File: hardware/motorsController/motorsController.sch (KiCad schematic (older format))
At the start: 10 parts, among them J1 batery_connector, J2 Screw_Terminal_01x01, J3 Screw_Terminal_01x01, J4 Screw_Terminal_01x01, J5 Screw_Terminal_01x01, J6 Screw_Terminal_01x01, J7 Screw_Terminal_01x01, J8 Screw_Terminal_01x01, J9 Screw_Terminal_01x01

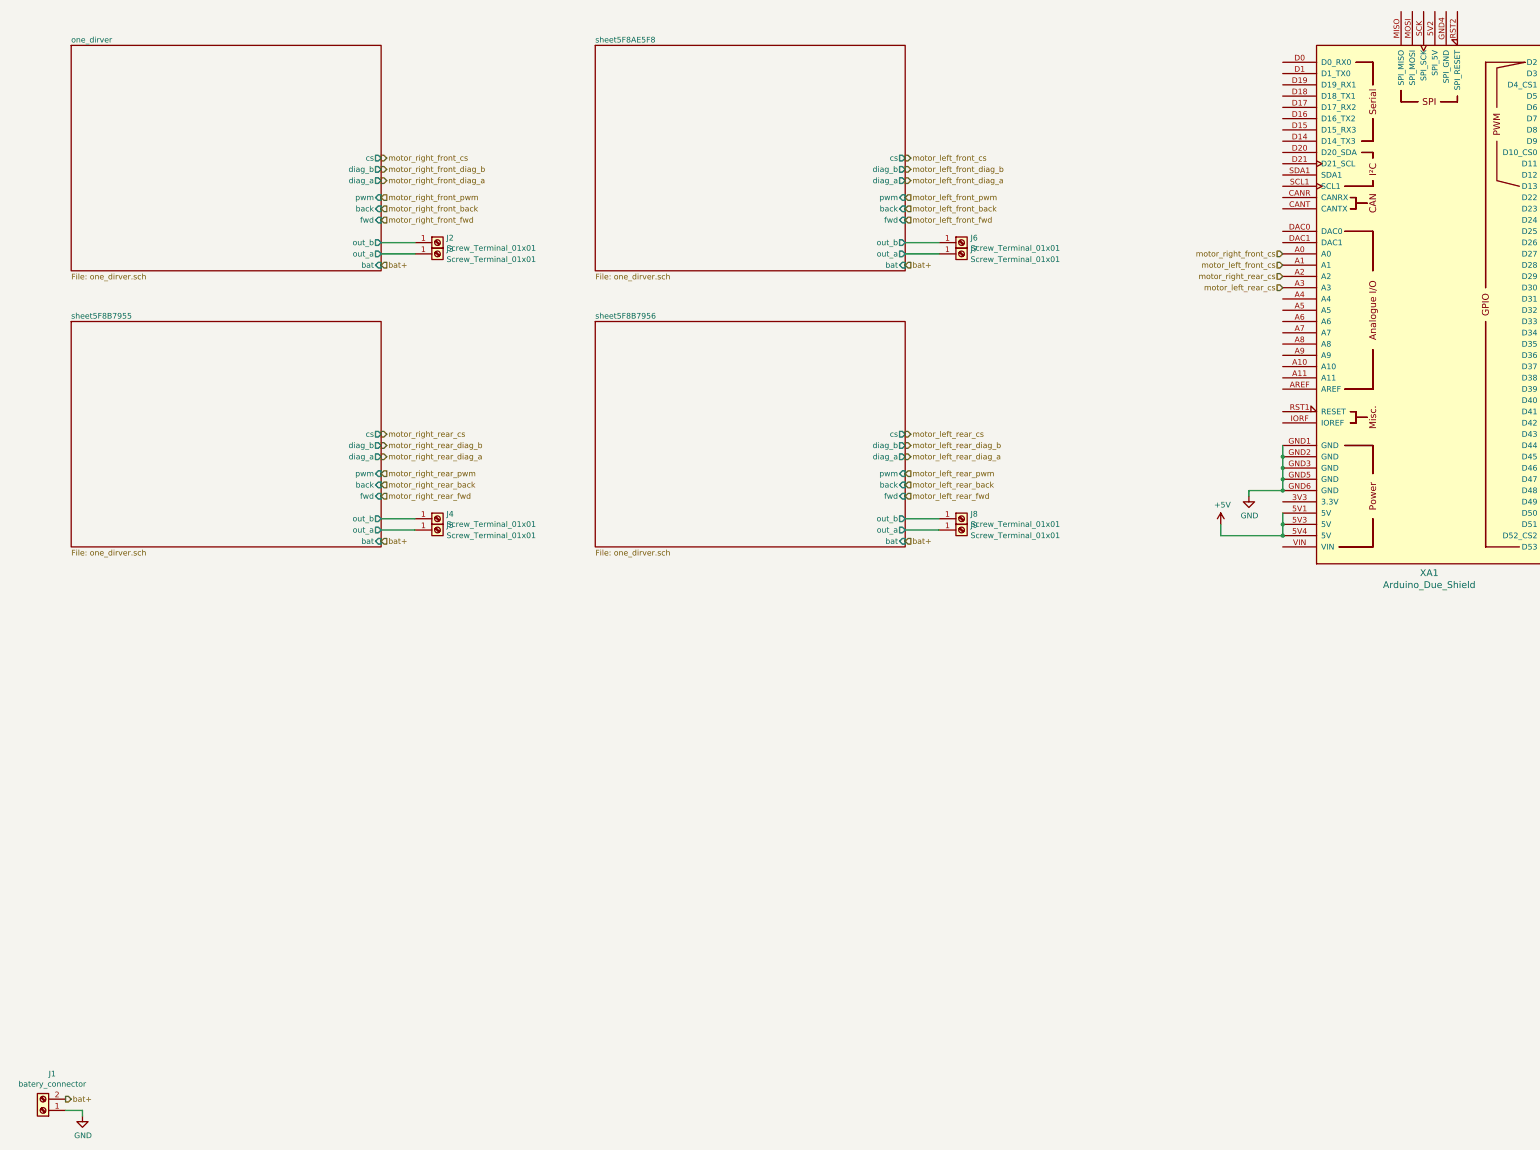
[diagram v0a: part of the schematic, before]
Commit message: layout and connect power for a pair of drivers
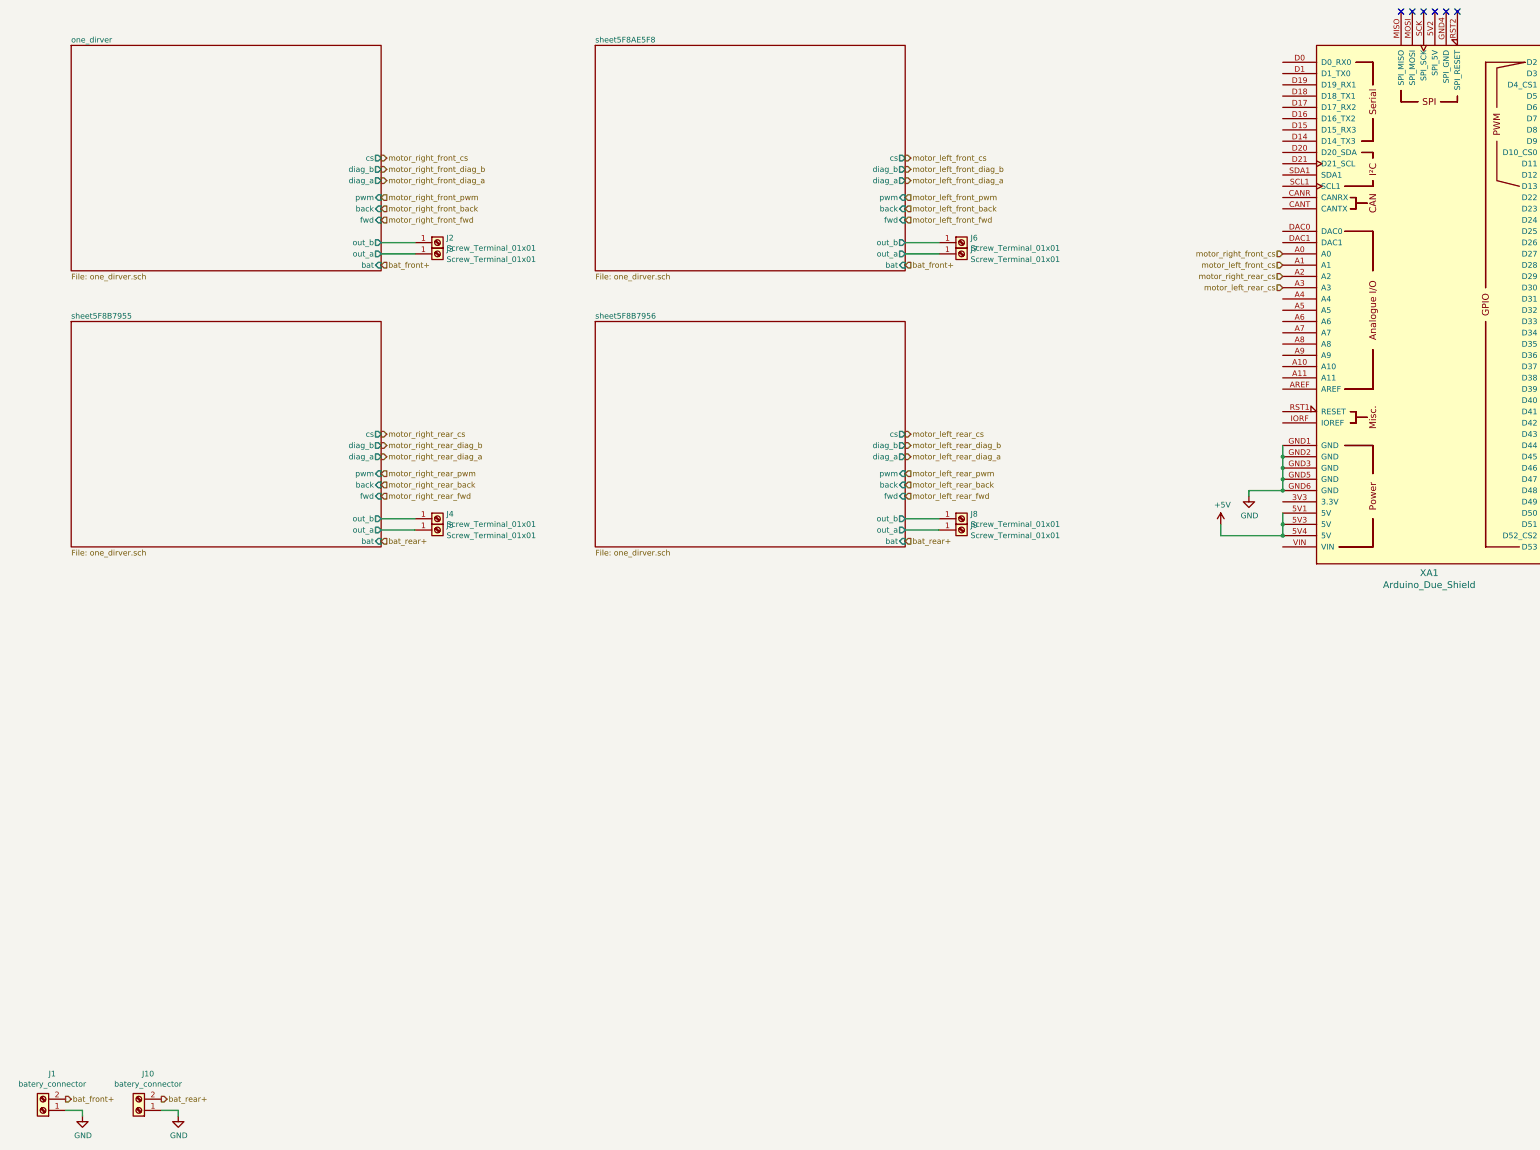
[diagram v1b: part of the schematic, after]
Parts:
- added J10: batery_connector, TerminalBlock:TerminalBlock_bornier-2_P5.08mm, symbol Connector:Screw_Terminal_01x02
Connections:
- net GND: now also J10.1 (Pin_1)
- net bat+ renamed bat_front+
- new net bat_rear+: J10.2 (Pin_2)
- no-connect marks 0 -> 6
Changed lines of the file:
@@
 	1350 10650 1200 10650
 Text HLabel 1200 10550 2    50   Output ~ 0
-bat+
+bat_front+
 Text HLabel 4000 3150 2    50   Input ~ 0
-bat+
+bat_front+
 $Comp
 L arduino:Arduino_Due_Shield XA1
@@
 motor_left_front_diag_a
 Text HLabel 8650 3150 2    50   Input ~ 0
-bat+
+bat_front+
 $Comp
 L Connector:Screw_Terminal_01x01 J6
@@
 motor_right_rear_diag_a
 Text HLabel 4000 5600 2    50   Input ~ 0
-bat+
+bat_rear+
 $Comp
 L Connector:Screw_Terminal_01x01 J4
@@
 motor_left_rear_diag_a
 Text HLabel 8650 5600 2    50   Input ~ 0
-bat+
+bat_rear+
 $Comp
 L Connector:Screw_Terminal_01x01 J8
@@
 Text HLabel 14600 1650 2    50   Output ~ 0
 motor_left_rear_pwm
+$Comp
+L Connector:Screw_Terminal_01x02 J10
+U 1 1 5F8FE7B8
+P 1850 10650
+F 0 "J10" H 1768 10325 50  0000 C CNN
+F 1 "batery_connector" H 1768 10416 50  0000 C CNN
+F 2 "TerminalBlock:TerminalBlock_bornier-2_P5.08mm" H 1850 10650 50  0001 C CNN
+F 3 "~" H 1850 10650 50  0001 C CNN
+	1    1850 10650
+	-1   0    0    1
+$EndComp
+$Comp
+L power:GND #PWR0120
+U 1 1 5F8FE7BE
+P 2200 10700
+F 0 "#PWR0120" H 2200 10450 50  0001 C CNN
+F 1 "GND" H 2205 10527 50  0000 C CNN
+F 2 "" H 2200 10700 50  0001 C CNN
+F 3 "" H 2200 10700 50  0001 C CNN
+	1    2200 10700
+	1    0    0    -1
+$EndComp
+Wire Wire Line
+	2200 10700 2200 10650
+Wire Wire Line
+	2200 10650 2050 10650
+Text HLabel 2050 10550 2    50   Output ~ 0
+bat_rear+
+NoConn ~ 13050 900
+NoConn ~ 13150 900
+NoConn ~ 13250 900
+NoConn ~ 13350 900
+NoConn ~ 13450 900
+NoConn ~ 13550 900
 $EndSCHEMATC

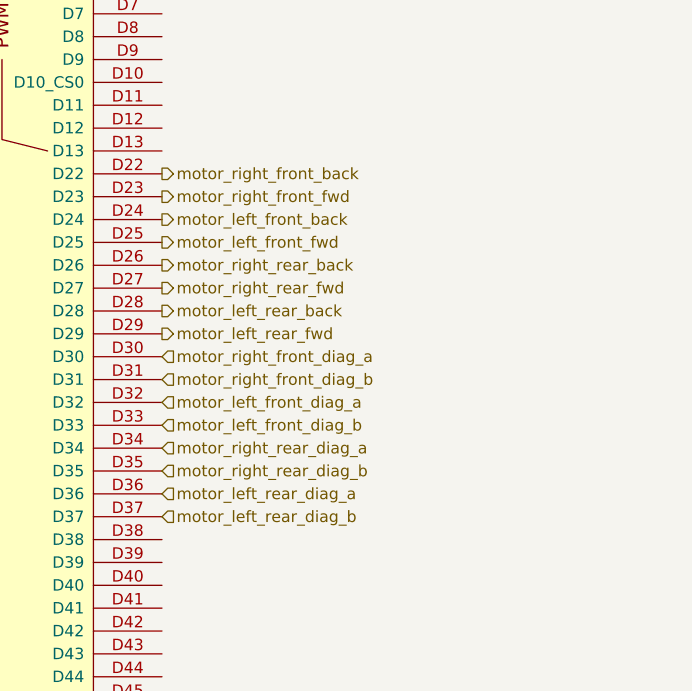
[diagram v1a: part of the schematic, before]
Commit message: connect left-rear driver to arduino
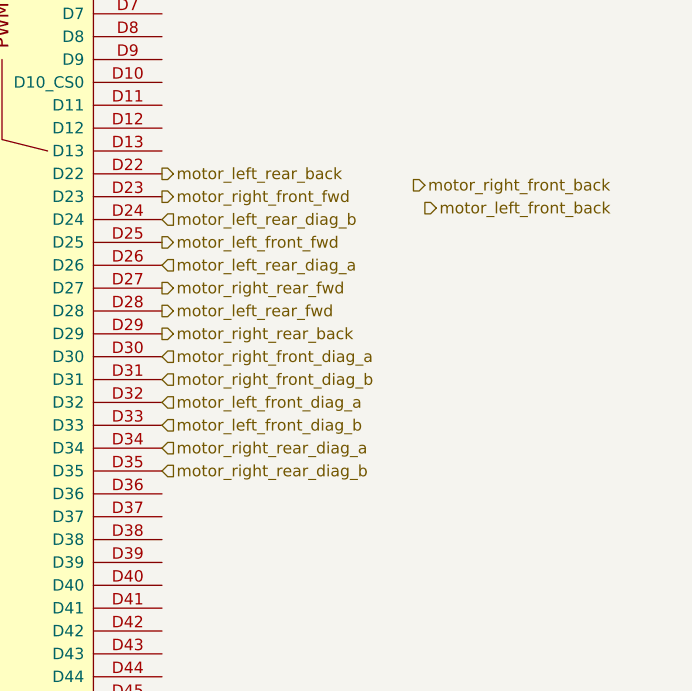
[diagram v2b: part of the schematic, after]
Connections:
- net motor_left_front_back: no longer XA1.D24
- net motor_left_rear_back: now also XA1.D22; no longer XA1.D28
- net motor_left_rear_diag_a: now also XA1.D26; no longer XA1.D36
- net motor_left_rear_diag_b: now also XA1.D24; no longer XA1.D37
- net motor_left_rear_fwd: now also XA1.D28; no longer XA1.D29
- net motor_right_front_back: no longer XA1.D22
- net motor_right_rear_back: now also XA1.D29; no longer XA1.D26
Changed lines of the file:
@@
 Text HLabel 14600 1350 2    50   Output ~ 0
 motor_right_front_pwm
-Text HLabel 14600 2550 2    50   Output ~ 0
+Text HLabel 15700 2600 2    50   Output ~ 0
 motor_right_front_back
 Text HLabel 14600 2650 2    50   Output ~ 0
@@
 Text HLabel 12000 3350 0    50   Input ~ 0
 motor_left_rear_cs
-Text HLabel 14600 2750 2    50   Output ~ 0
+Text HLabel 15750 2700 2    50   Output ~ 0
 motor_left_front_back
 Text HLabel 14600 2850 2    50   Output ~ 0
 motor_left_front_fwd
-Text HLabel 14600 2950 2    50   Output ~ 0
+Text HLabel 14600 3250 2    50   Output ~ 0
 motor_right_rear_back
 Text HLabel 14600 3050 2    50   Output ~ 0
 motor_right_rear_fwd
+Text HLabel 14600 2550 2    50   Output ~ 0
+motor_left_rear_back
 Text HLabel 14600 3150 2    50   Output ~ 0
-motor_left_rear_back
-Text HLabel 14600 3250 2    50   Output ~ 0
 motor_left_rear_fwd
 Text HLabel 14600 3650 2    50   Input ~ 0
@@
 Text HLabel 14600 3750 2    50   Input ~ 0
 motor_right_rear_diag_a
-Text HLabel 14600 4050 2    50   Input ~ 0
-motor_left_rear_diag_b
-Text HLabel 14600 3950 2    50   Input ~ 0
-motor_left_rear_diag_a
 Text HLabel 14600 1450 2    50   Output ~ 0
 motor_left_front_pwm
@@
 NoConn ~ 13450 900
 NoConn ~ 13550 900
+Text HLabel 14600 2750 2    50   Input ~ 0
+motor_left_rear_diag_b
+Text HLabel 14600 2950 2    50   Input ~ 0
+motor_left_rear_diag_a
 $EndSCHEMATC

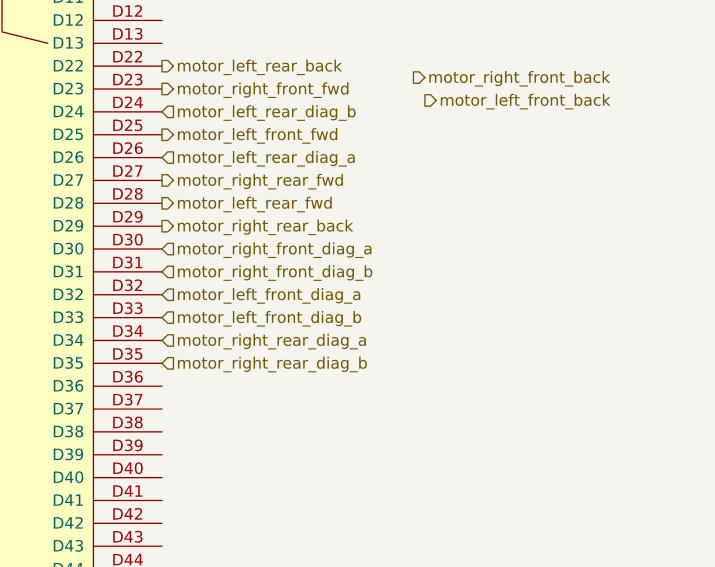
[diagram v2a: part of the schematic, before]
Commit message: reconnect right-rear driver to more conenient pins
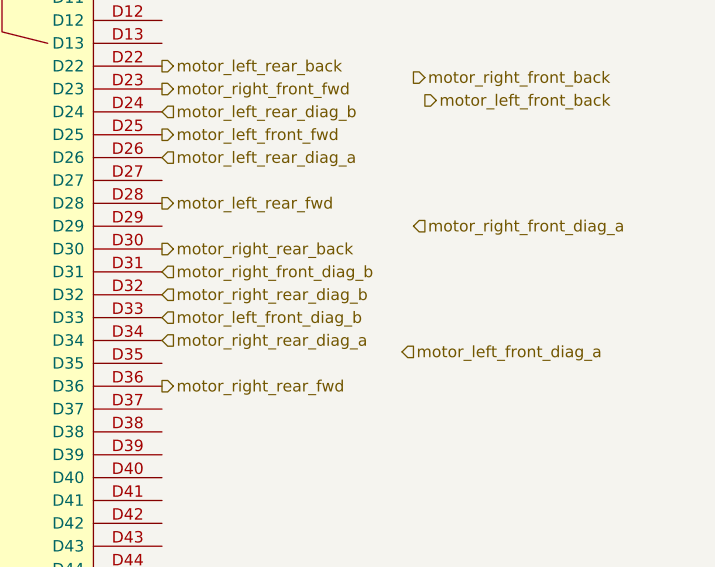
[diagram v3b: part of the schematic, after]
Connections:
- net motor_left_front_diag_a: no longer XA1.D32
- net motor_right_front_diag_a: no longer XA1.D30
- net motor_right_rear_back: now also XA1.D30; no longer XA1.D29
- net motor_right_rear_diag_b: now also XA1.D32; no longer XA1.D35
- net motor_right_rear_fwd: now also XA1.D36; no longer XA1.D27
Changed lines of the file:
@@
 Text HLabel 14600 3450 2    50   Input ~ 0
 motor_right_front_diag_b
-Text HLabel 14600 3350 2    50   Input ~ 0
+Text HLabel 15700 3250 2    50   Input ~ 0
 motor_right_front_diag_a
 $Comp
@@
 Text HLabel 14600 2850 2    50   Output ~ 0
 motor_left_front_fwd
-Text HLabel 14600 3250 2    50   Output ~ 0
-motor_right_rear_back
-Text HLabel 14600 3050 2    50   Output ~ 0
+Text HLabel 14600 3950 2    50   Output ~ 0
 motor_right_rear_fwd
 Text HLabel 14600 2550 2    50   Output ~ 0
@@
 Text HLabel 14600 3650 2    50   Input ~ 0
 motor_left_front_diag_b
+Text HLabel 15650 3800 2    50   Input ~ 0
+motor_left_front_diag_a
 Text HLabel 14600 3550 2    50   Input ~ 0
-motor_left_front_diag_a
-Text HLabel 14600 3850 2    50   Input ~ 0
 motor_right_rear_diag_b
 Text HLabel 14600 3750 2    50   Input ~ 0
@@
 Text HLabel 14600 2950 2    50   Input ~ 0
 motor_left_rear_diag_a
+Text HLabel 14600 3350 2    50   Output ~ 0
+motor_right_rear_back
 $EndSCHEMATC

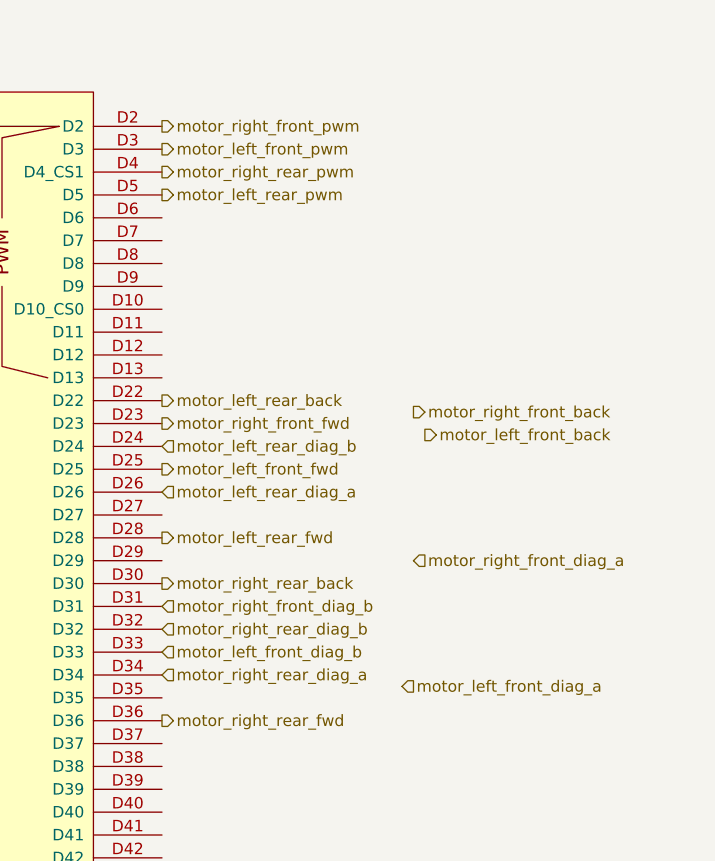
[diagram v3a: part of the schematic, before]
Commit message: connect left-front driver to arduino
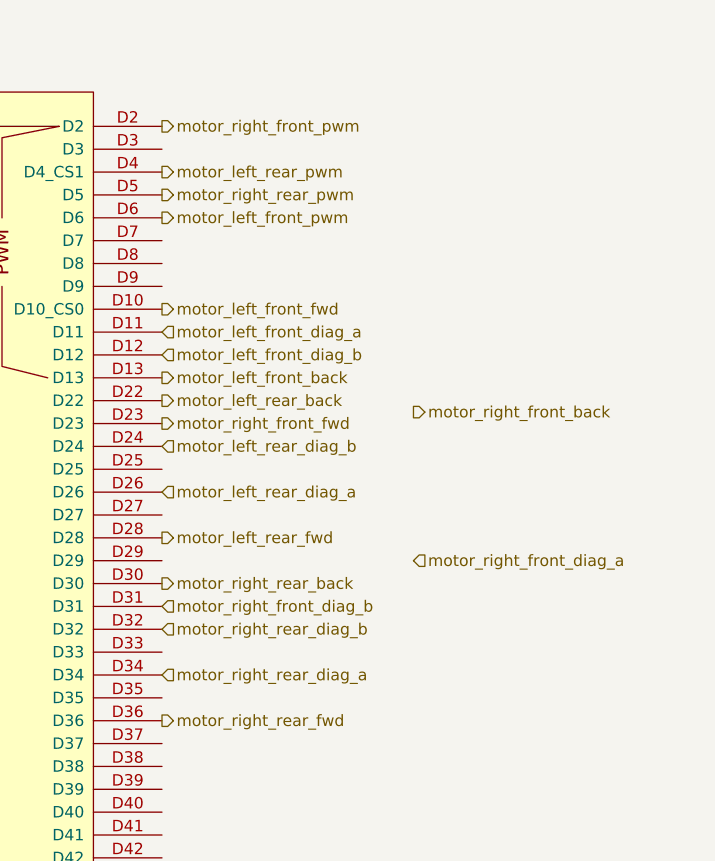
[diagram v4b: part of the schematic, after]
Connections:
- net motor_left_front_back: now also XA1.D13
- net motor_left_front_diag_a: now also XA1.D11
- net motor_left_front_diag_b: now also XA1.D12; no longer XA1.D33
- net motor_left_front_fwd: now also XA1.D10 (D10_CS0); no longer XA1.D25
- net motor_left_front_pwm: now also XA1.D6; no longer XA1.D3
- net motor_left_rear_pwm: now also XA1.D4 (D4_CS1); no longer XA1.D5
- net motor_right_rear_pwm: now also XA1.D5; no longer XA1.D4 (D4_CS1)
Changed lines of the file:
@@
 Text HLabel 12000 3350 0    50   Input ~ 0
 motor_left_rear_cs
-Text HLabel 15750 2700 2    50   Output ~ 0
+Text HLabel 14600 2450 2    50   Output ~ 0
 motor_left_front_back
-Text HLabel 14600 2850 2    50   Output ~ 0
+Text HLabel 14600 2150 2    50   Output ~ 0
 motor_left_front_fwd
 Text HLabel 14600 3950 2    50   Output ~ 0
@@
 Text HLabel 14600 3150 2    50   Output ~ 0
 motor_left_rear_fwd
-Text HLabel 14600 3650 2    50   Input ~ 0
+Text HLabel 14600 2350 2    50   Input ~ 0
 motor_left_front_diag_b
-Text HLabel 15650 3800 2    50   Input ~ 0
+Text HLabel 14600 2250 2    50   Input ~ 0
 motor_left_front_diag_a
 Text HLabel 14600 3550 2    50   Input ~ 0
@@
 Text HLabel 14600 3750 2    50   Input ~ 0
 motor_right_rear_diag_a
-Text HLabel 14600 1450 2    50   Output ~ 0
+Text HLabel 14600 1750 2    50   Output ~ 0
 motor_left_front_pwm
+Text HLabel 14600 1650 2    50   Output ~ 0
+motor_right_rear_pwm
 Text HLabel 14600 1550 2    50   Output ~ 0
-motor_right_rear_pwm
-Text HLabel 14600 1650 2    50   Output ~ 0
 motor_left_rear_pwm
 $Comp
